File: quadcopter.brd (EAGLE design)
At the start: 136.9 x 137 mm, 62 parts, among them J1 AVR_SPI_PRG_6NS, U1 ATMEGA128RFA1, Y1 16MHz

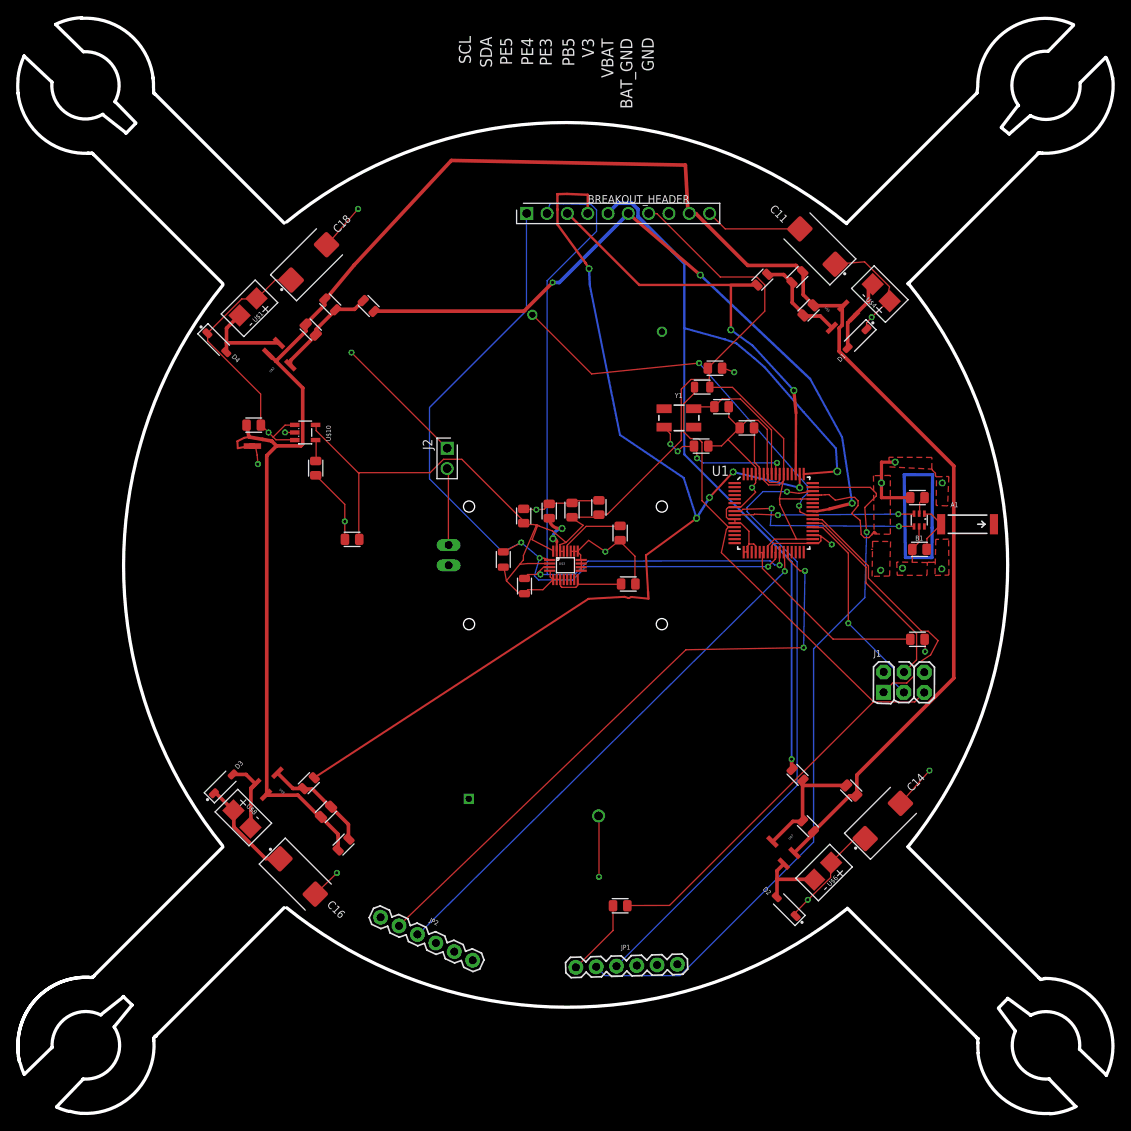
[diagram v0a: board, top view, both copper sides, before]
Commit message: Finished All Air-wires, the remaining airwires are already connected yet wishes to connect to others of the same connection. Need to ask
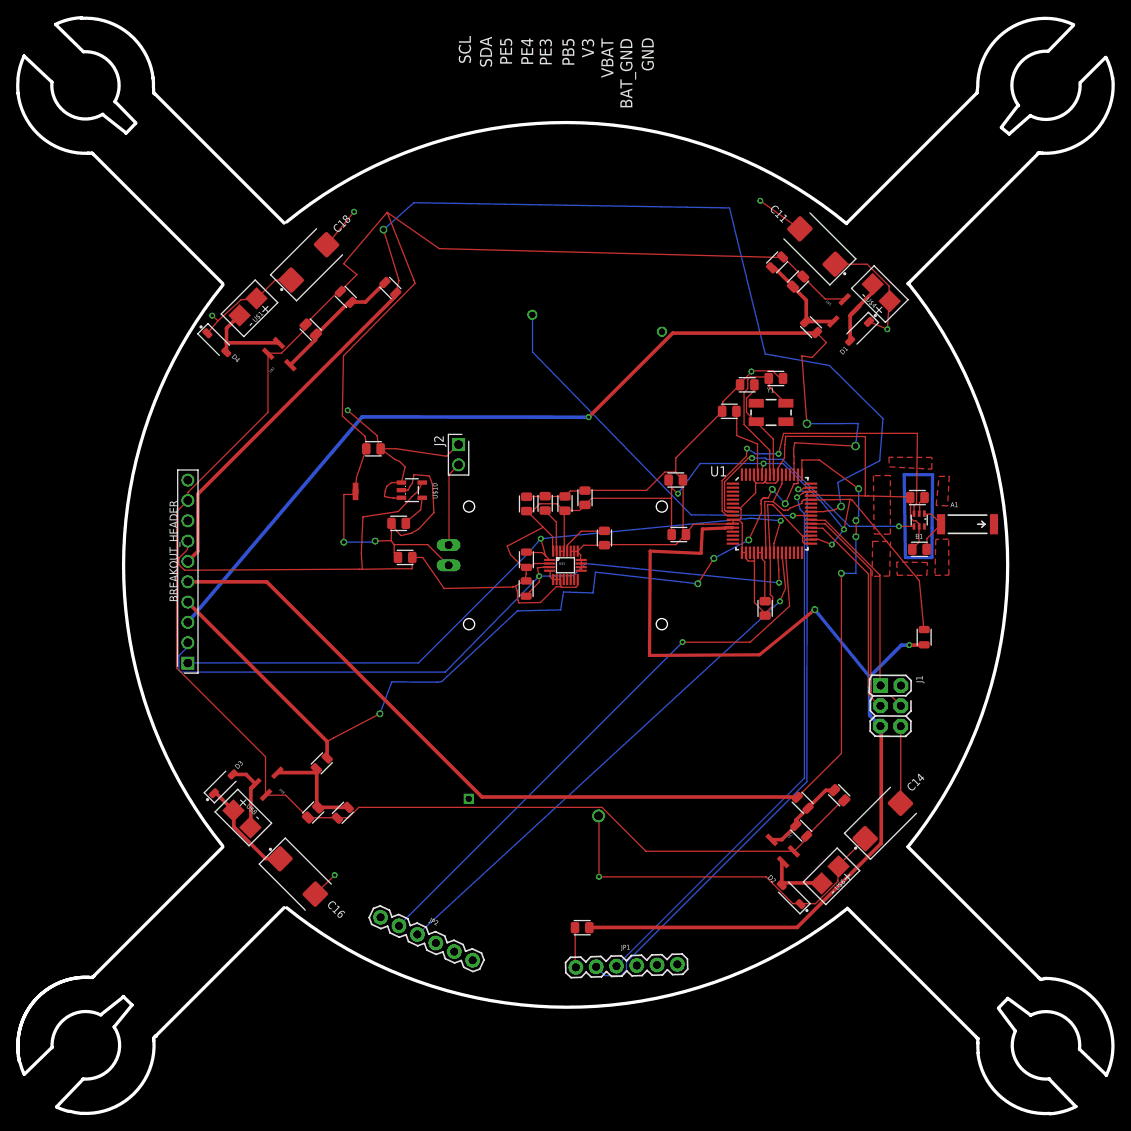
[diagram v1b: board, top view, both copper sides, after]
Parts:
- moved BREAKOUT_HEADER 70.4 mm to (-47.2, -12.2), turned to 90 degrees
- moved R1 41.8 mm to (44.8, -8.98), turned to 90 degrees
- moved C28 19.4 mm to (25.0, -5.38), turned to 270 degrees
- moved C25 15.3 mm to (-24.0, 14.6)
- moved U$10 15.2 mm to (-19.2, 9.40)
- moved C6 14.8 mm to (13.8, 10.7)
- moved U$11 14.1 mm to (-26.2, 9.37), turned to 90 degrees
- moved C23 12.5 mm to (-20.9, 5.25), turned to 180 degrees
- moved Y1 11.5 mm to (25.7, 19.1)
- moved C26 9.58 mm to (22.7, 22.6), turned to 180 degrees
- moved C5 8.84 mm to (14.2, 3.85)
- moved R4 8.51 mm to (30.7, 29.8), turned to 135 degrees
- moved C27 7.65 mm to (26.3, 23.4)
- moved C24 7.00 mm to (-20.0, 0.99)
- moved C10 5.48 mm to (2.09, -45.3)
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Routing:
- net GND: track 156.1 -> 235.5 mm, vias 18 -> 6
- net PE5: track 58.9 -> 129.9 mm, vias 2 -> 3
- net PB5: track 89.3 -> 151.7 mm, vias 3 -> 2
- net RESET: track 100.0 -> 130.5 mm, vias 0 -> 2
- net PE3: track 114.6 -> 140.2 mm, vias 2 -> 4
- net PE4: track 132.2 -> 107.4 mm, vias 5 -> 6
- net N$37: track 22.5 -> 44.4 mm
- net N$41: track 24.8 -> 6.74 mm
- net V3: track 194.7 -> 212.5 mm, vias 0 -> 4
- net VBAT: track 90.4 -> 107.6 mm, vias 5 -> 4
- net TX0: track 89.7 -> 76.5 mm
- net BAT_GND: track 260.9 -> 271.2 mm
- net N$36: track 24.8 -> 33.1 mm
- net RX0: track 78.3 -> 70.5 mm
- net MISO: track 33.2 -> 25.4 mm
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
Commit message: No more errorsgit add quadcopter.brd
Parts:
- moved U$11 2.62 mm to (-23.8, 8.47)
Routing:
- net V3: track 212.5 -> 215.8 mm
- net SCK: track 26.8 -> 28.8 mm
- net MISO: track 25.4 -> 26.7 mm
- net VBAT: track 107.6 -> 106.5 mm
- net BAT_GND: track 271.2 -> 272.0 mm
- net MOSI: track 29.7 -> 30.6 mm
- net GND: track 235.5 -> 234.7 mm, vias 6 -> 12
- net N$37: track 44.4 -> 43.7 mm, vias 2 -> 4
- net RESET: track 130.5 -> 130.0 mm
